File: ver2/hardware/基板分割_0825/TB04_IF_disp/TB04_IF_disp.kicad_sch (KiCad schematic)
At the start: 12 parts, among them J101 USB_C_Receptacle_PowerOnly_6P, SW101 SW_SPDT, U101 74LS157, U102 74HC138

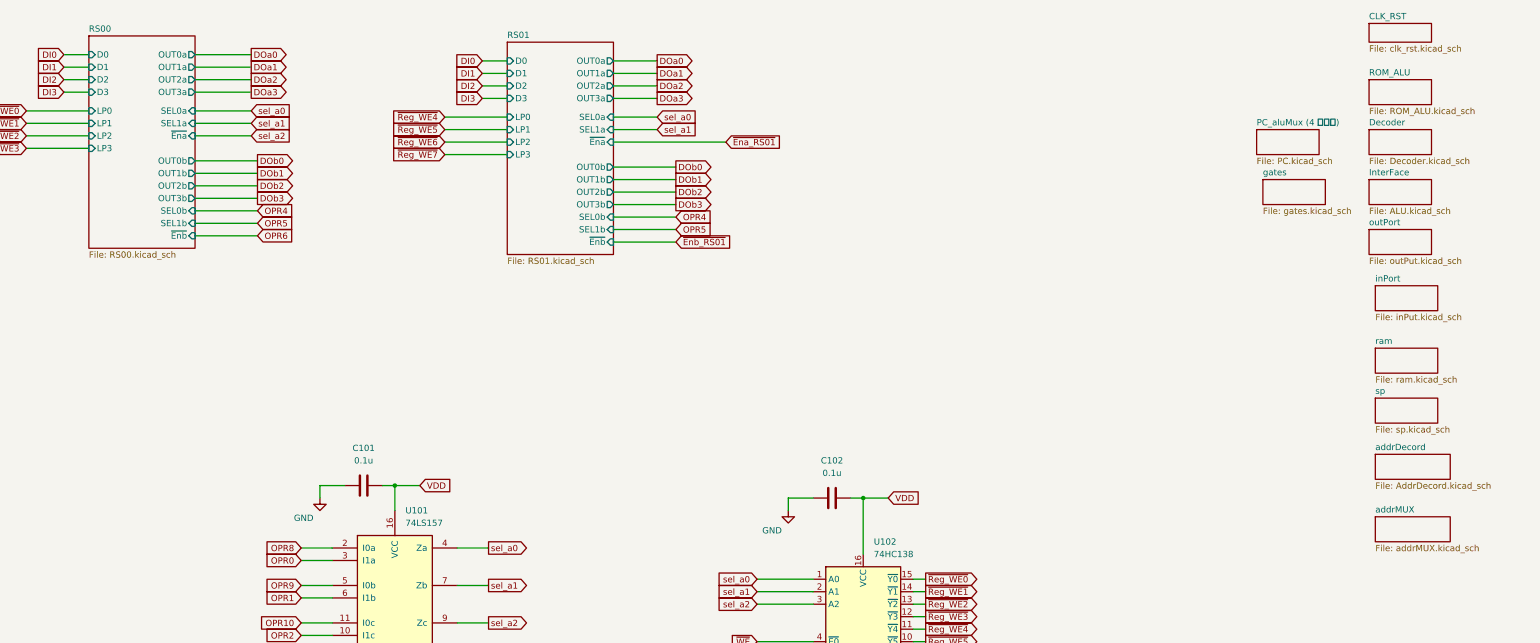
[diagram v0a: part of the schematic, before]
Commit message: ver2: 残り5プロジェクトの不要シートを一括削除
IF表示13/S4 10/S3 11/S1 12/S2 10枚のsheetブロックをS式単位で除去し、
対応する子シート56ファイルを削除。部分削除が要るROM_ALU・PCは残した。
残ったブロックは全てHEADとバイト一致・括弧バランス0を全数確認。

Co-Authored-By: Claude Opus 5 <noreply@anthropic.com>
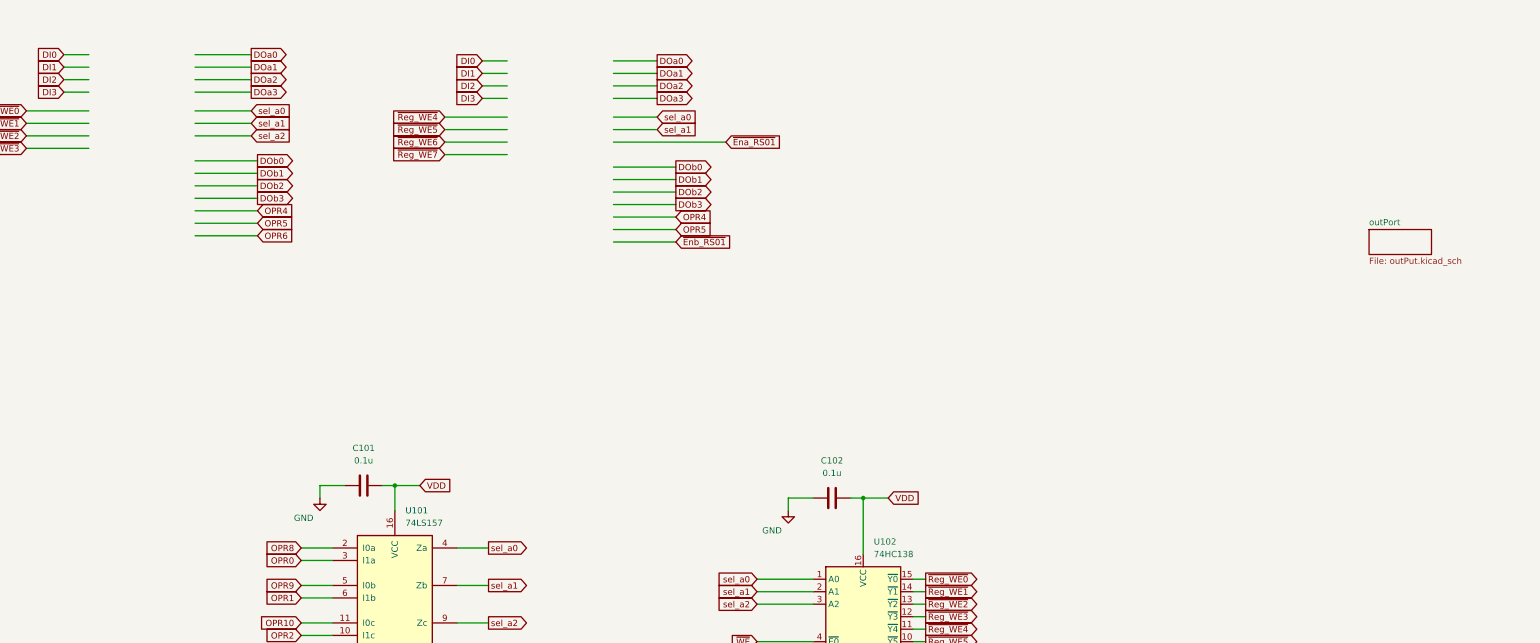
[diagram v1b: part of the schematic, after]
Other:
- removed sheet CLK_RST
- removed sheet Decoder
- removed sheet InterFace
- removed sheet PC_aluMux (4 ページ)
- removed sheet ROM_ALU
- removed sheet RS00
- removed sheet RS01
- removed sheet addrDecord
- removed sheet addrMUX
- removed sheet gates
- removed sheet inPort
- removed sheet ram
- removed sheet sp

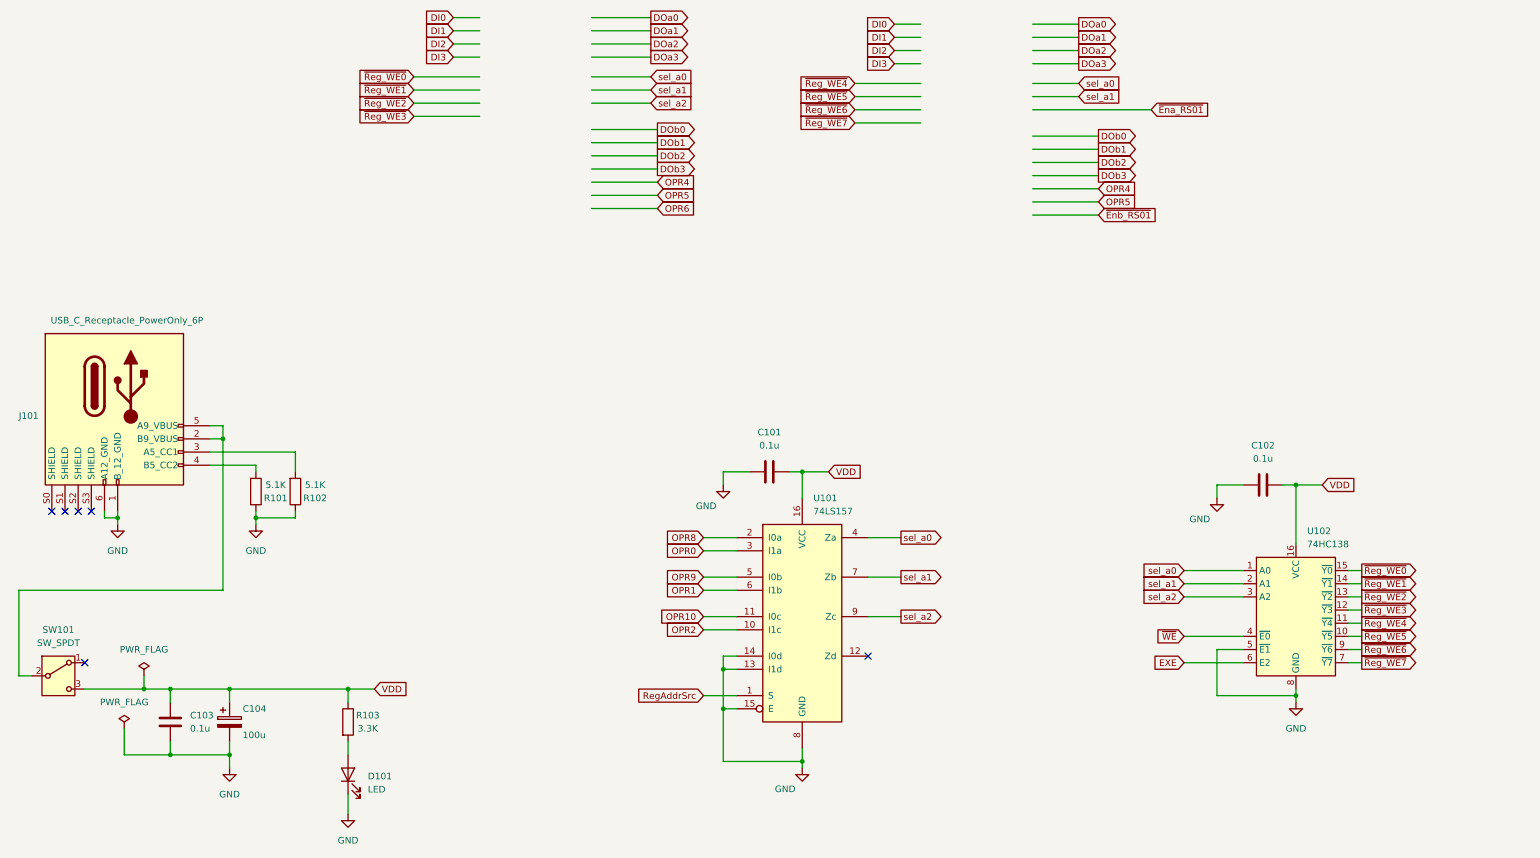
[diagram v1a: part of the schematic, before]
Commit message: ver2: S1-S4にバスヘッダ3本を実装(120ピン全数一致)／S4にIF向け20ピン3個
J101-103は4枚とも確定表と全120ピン一致。J104(IF入力)/J105(IF表示)/
J106(キャリアB)も20ピン全一致。コネクタ以外の署名はマスターと相違0で、
コネクタ追加時のワイヤ吸着なし。PC_Qはバスに載せずJ106のみ。

Co-Authored-By: Claude Opus 5 <noreply@anthropic.com>
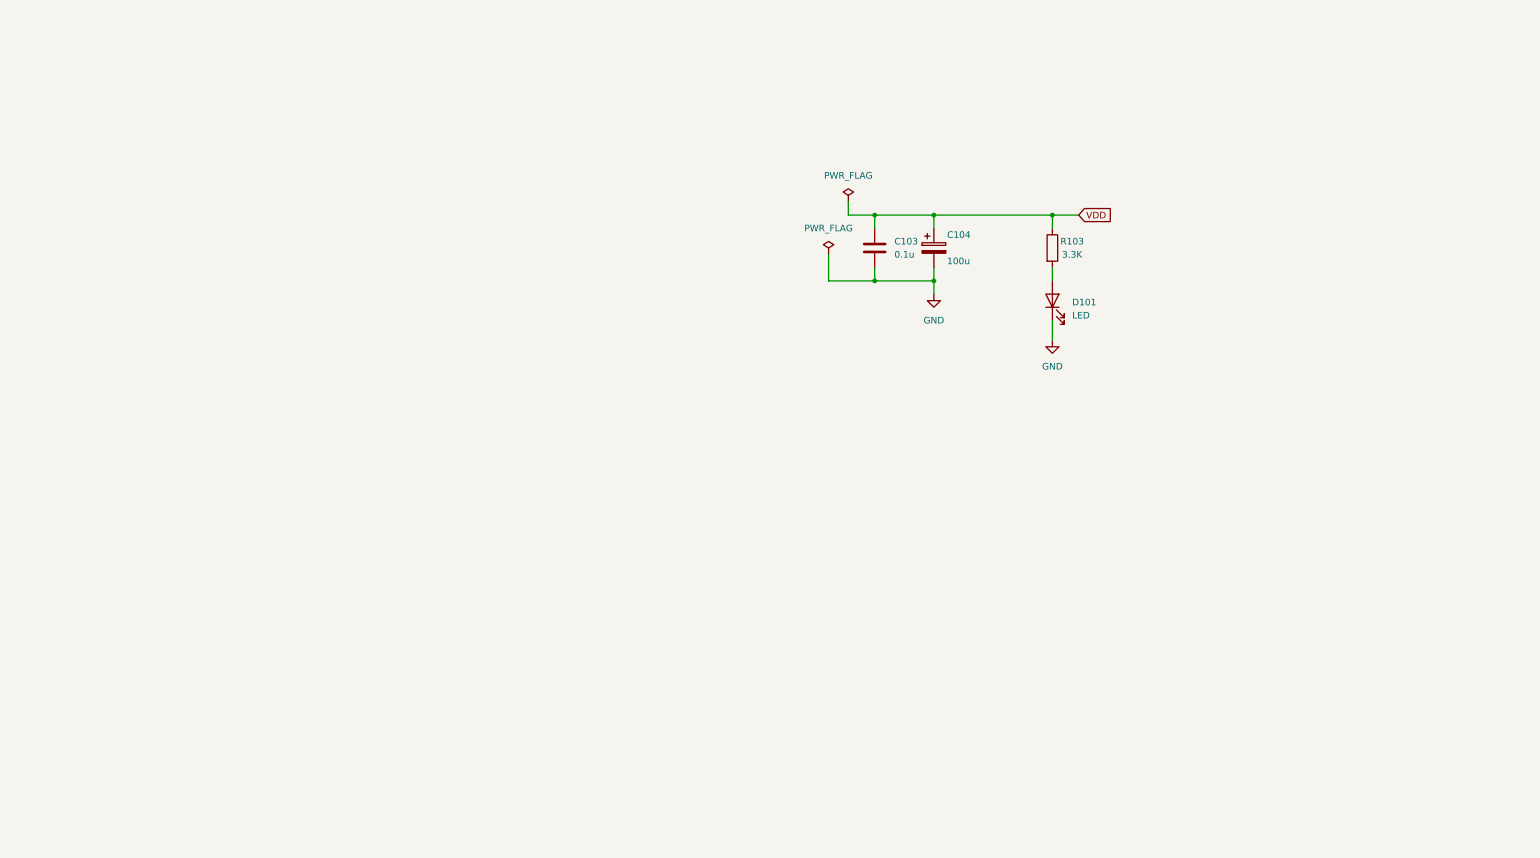
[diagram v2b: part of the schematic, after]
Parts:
- removed C101, C102: 0.1u, Capacitor_THT:C_Disc_D4.3mm_W1.9mm_P5.00mm, symbol Device:C
- removed J101: USB_C_Receptacle_PowerOnly_6P, Library:USB_C_receptacle_onlypower_tanuki, symbol New_Library:USB_C_Receptacle_PowerOnly_6P_tanuki
- removed R101, R102: 5.1K, Resistor_THT:R_Axial_DIN0207_L6.3mm_D2.5mm_P10.16mm_Horizontal, symbol Device:R
- removed SW101: SW_SPDT, Library:sw_slide, symbol Switch:SW_SPDT
- removed U101: 74LS157, symbol 74xx:74LS157
- removed U102: 74HC138, Package_DIP:DIP-16_W7.62mm_Socket, symbol 74xx:74HC138
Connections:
- no-connect marks 6 -> 0
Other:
- moved on the sheet: C103, C104, D101, R103

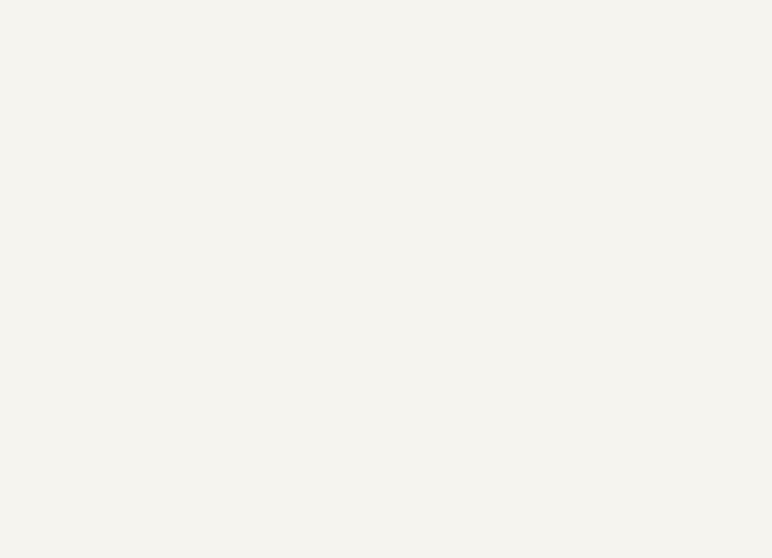
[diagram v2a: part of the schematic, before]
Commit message: ver2: IF2枚とキャリアにコネクタを実装(ピン配置は表と全一致)
IF入力J104(20)・IF表示J105(20)・キャリアJ1(20)を突合し不一致ゼロ。
IF入力の電源経路(USB-C→SW101→VDD→J104 pin18-20)も確認。
3プロジェクトともANOMALIES 0。

Co-Authored-By: Claude Opus 5 <noreply@anthropic.com>
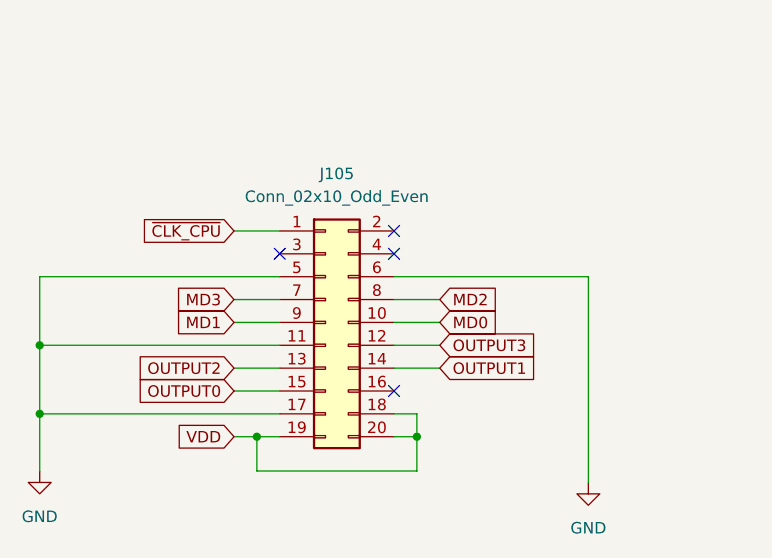
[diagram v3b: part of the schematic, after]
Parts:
- added J105: Conn_02x10_Odd_Even, symbol Connector_Generic:Conn_02x10_Odd_Even
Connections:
- net GND: now also J105.11 (Pin_11), J105.17 (Pin_17), J105.5 (Pin_5), J105.6 (Pin_6)
- net VDD: now also J105.18 (Pin_18), J105.19 (Pin_19), J105.20 (Pin_20)
- new net MD0: J105.10 (Pin_10)
- new net MD1: J105.9 (Pin_9)
- new net MD2: J105.8 (Pin_8)
- new net MD3: J105.7 (Pin_7)
- new net OUTPUT0: J105.15 (Pin_15)
- new net OUTPUT1: J105.14 (Pin_14)
- new net OUTPUT2: J105.13 (Pin_13)
- new net OUTPUT3: J105.12 (Pin_12)
- new net ~{CLK_CPU}: J105.1 (Pin_1)
- no-connect marks 0 -> 4

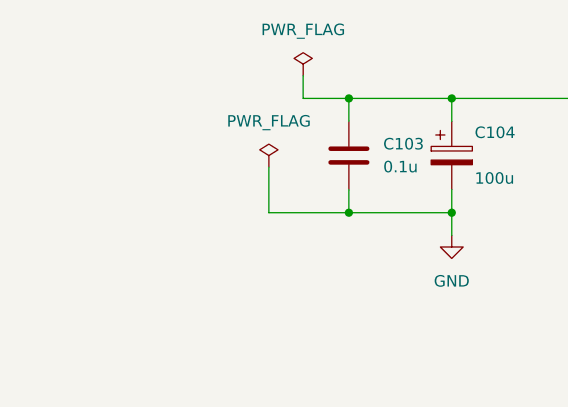
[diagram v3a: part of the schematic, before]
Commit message: ver2: キャリアに7segIF用2×5コネクタ4個と電源部を実装／全7枚に予備の端子台
- キャリア: J3-J6(2×5)が桁1-4で表と全一致・DIG_*16ネットは2ピン構成
  (isolated_pin_label 16件→0件)、C1/C2/電源LED/端子台を追加
- 入力の2×10はJ1→J2にリナンバー(20ピンの中身は表と一致)
- 7枚とも端子台J1602を1個ずつ追加(pin1=＋/pin2=GNDで向きは全枚統一)
- 署名比較で既存ピンのネット変化は7枚とも0件(吸着なし)

Co-Authored-By: Claude Opus 5 <noreply@anthropic.com>
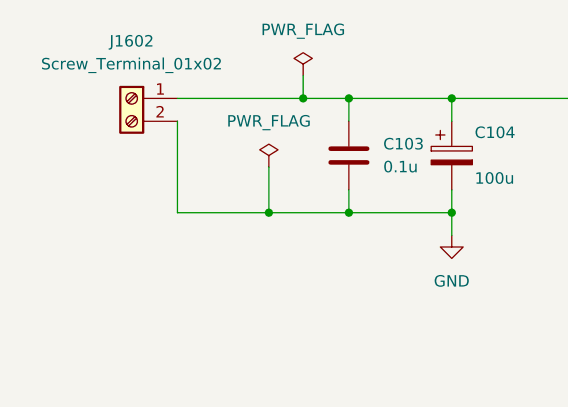
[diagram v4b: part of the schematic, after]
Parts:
- added J1602: Screw_Terminal_01x02, symbol Connector:Screw_Terminal_01x02
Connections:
- net GND: now also J1602.2 (Pin_2)
- net VDD: now also J1602.1 (Pin_1)
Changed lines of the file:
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@@
+	)
+	(junction
+		(at 176.53 81.28)
+		(diameter 0)
+		(color 0 0 0 0)
 	)
 	(junction
@@
 		(color 0 0 0 0)
 	)
+	(junction
+		(at 180.34 68.58)
+		(diameter 0)
+		(color 0 0 0 0)
+	)
 	(no_connect
 		(at 196.85 156.21)
@@
 	(wire
 		(pts
+			(xy 166.37 68.58) (xy 180.34 68.58)
+		)
+		(stroke
+			(width 0)
+			(type default)
+		)
+	)
+	(wire
+		(pts
 			(xy 194.31 180.34) (xy 194.31 176.53)
 		)
@@
 	(wire
 		(pts
+			(xy 166.37 81.28) (xy 176.53 81.28)
+		)
+		(stroke
+			(width 0)
+			(type default)
+		)
+	)
+	(wire
+		(pts
 			(xy 176.53 76.2) (xy 176.53 81.28)
+		)
+		(stroke
+			(width 0)
+			(type default)
+		)
+	)
+	(wire
+		(pts
+			(xy 166.37 71.12) (xy 166.37 81.28)
 		)
 		(stroke
@@
 					(unit 1)
 				)
+			)
+		)
+	)
+	(symbol
+		(lib_id "Connector:Screw_Terminal_01x02")
+		(at 161.29 68.58 0)
+		(mirror y)
+		(unit 1)
+		(body_style 1)
+		(exclude_from_sim no)
+		(in_bom yes)
+		(on_board yes)
+		(in_pos_files yes)
+		(dnp no)
+		(fields_autoplaced yes)
+		(property "Reference" "J1602"
+			(at 161.29 62.23 0)
+			(show_name no)
+			(do_not_autoplace no)
+			(effects
+				(font
+					(size 1.27 1.27)
+				)
+			)
+		)
+		(property "Value" "Screw_Terminal_01x02"
+			(at 161.29 64.77 0)
+			(show_name no)
+			(do_not_autoplace no)
+			(effects
+				(font
+					(size 1.27 1.27)
+				)
+			)
+		)
+		(property "Footprint" ""
+			(at 161.29 68.58 0)
+			(hide yes)
+			(show_name no)
+			(do_not_autoplace no)
+			(effects
+				(font
+					(size 1.27 1.27)
+				)
+			)
+		)
+		(property "Datasheet" ""
+			(at 161.29 68.58 0)
+			(hide yes)
+			(show_name no)
+			(do_not_autoplace no)
+			(effects
+				(font
+					(size 1.27 1.27)
+				)
+			)
+		)
+		(property "Description" "Generic screw terminal, single row, 01x02, script generated (kicad-library-utils/schlib/autogen/connector/)"
+			(at 161.29 68.58 0)
+			(hide yes)
+			(show_name no)
+			(do_not_autoplace no)
+			(effects
+				(font
+					(size 1.27 1.27)
+				)
+			)
+		)
+		(pin "2"
+		)
+		(pin "1"
+		)
+		(instances
+			(project "TB04_IF_disp"
+				(path "/d176c79b-dced-4d01-bcec-7dfd676fcfc2"
+					(reference "J1602")
+					(unit 1)
+				)
